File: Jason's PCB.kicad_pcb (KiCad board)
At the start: 2 copper layers, 9 parts, among them U1 Elite-C

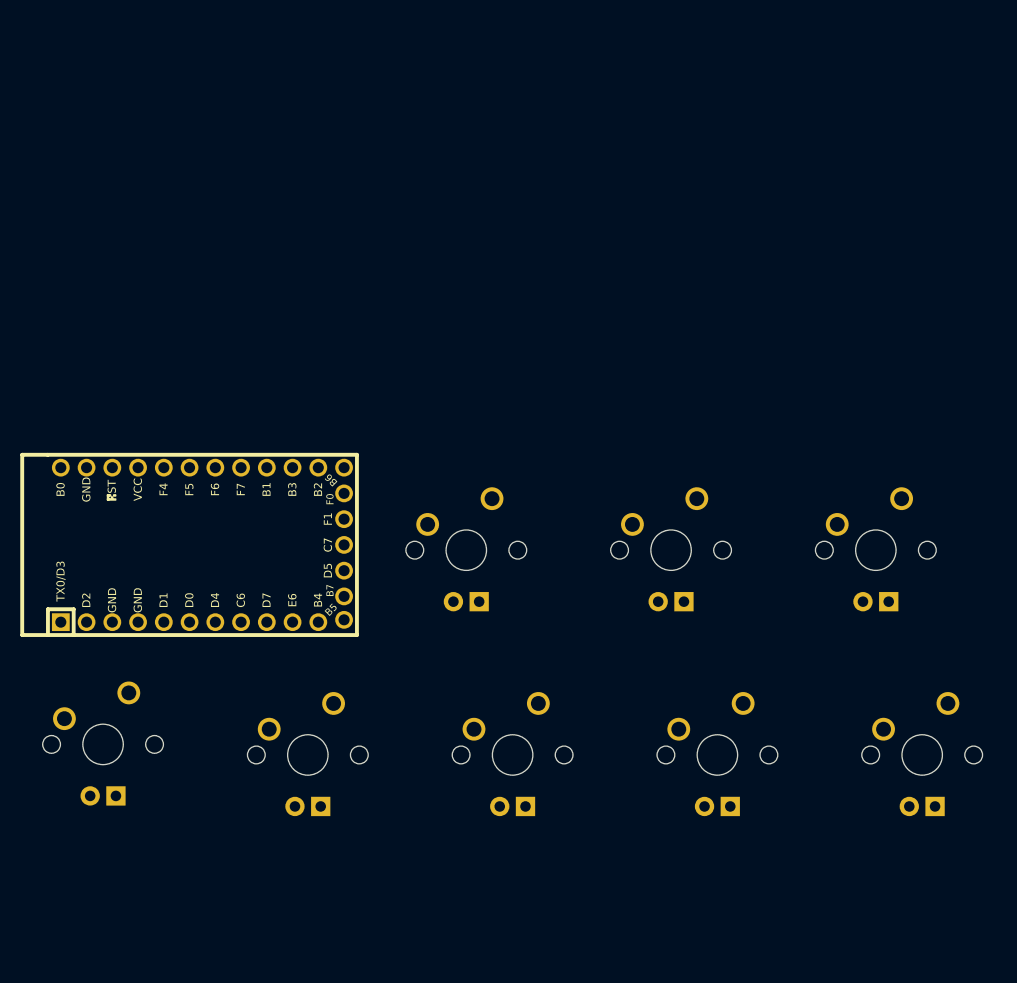
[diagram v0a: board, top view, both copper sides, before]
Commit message: Schematic/PCB General Shape
-Added 2 rotary encoder
-Simplified PCB. No need for diodes.
-Added outside edges of PCB
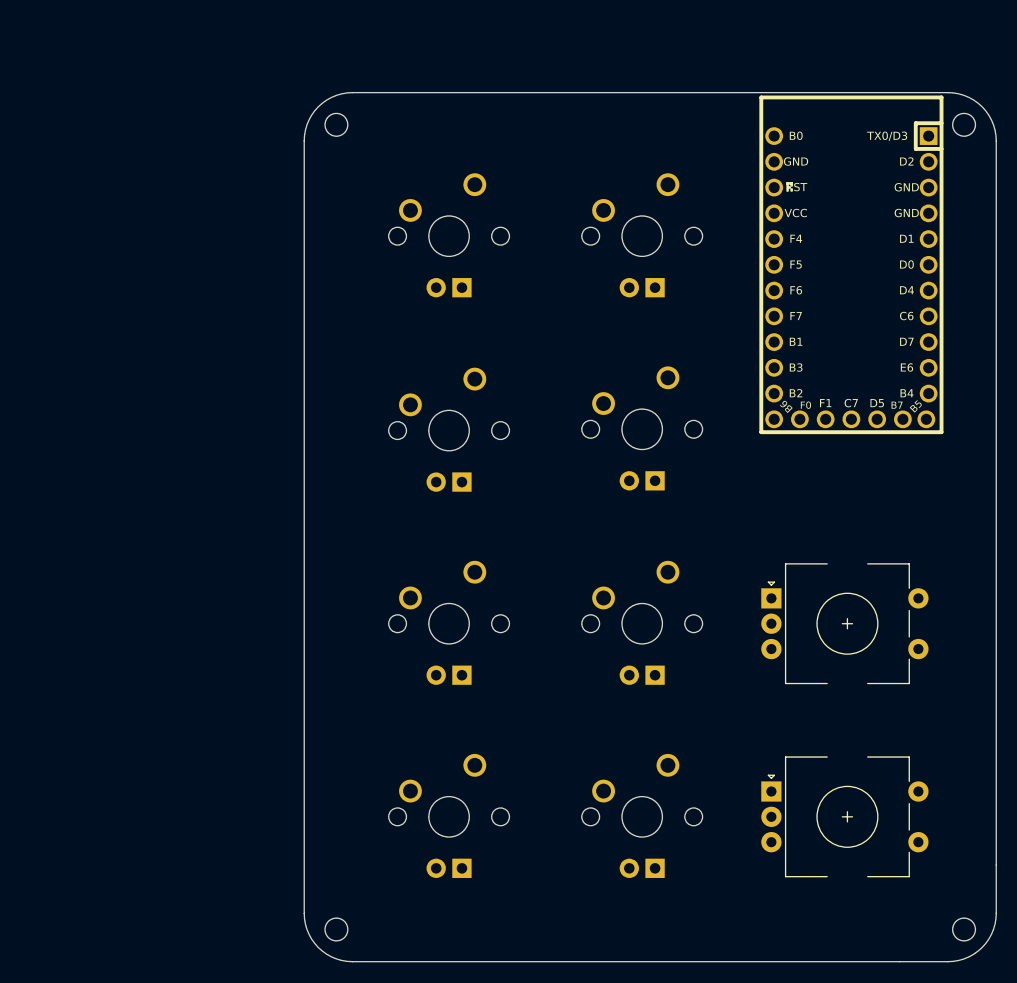
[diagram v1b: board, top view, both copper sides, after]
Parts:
- added SW_E1: Rotary_Encoder_Switch, Keebio-Parts:RotaryEncoder_EC11, F.Cu at (153.6, 73.0)
- added SW_E2: Rotary_Encoder_Switch, Keebio-Parts:RotaryEncoder_EC11, F.Cu at (153.6, 92.1)
- U1: moved to B.Cu
- moved U1 69.2 mm to (154.0, 38.9), turned to 270 degrees
- moved SW_A1 60.6 mm to (114.3, 34.8)
- moved SW_A2 35.5 mm to (133.3, 34.8)
- moved SW_B1 34.9 mm to (114.3, 54.0)
- moved SW_D2 28.3 mm to (133.3, 92.1)
- moved SW_D1 27.2 mm to (114.3, 92.1)
- moved SW_C2 24.2 mm to (133.3, 73.0)
- moved SW_C1 14.4 mm to (114.3, 73.0)
- moved SW_B2 12.3 mm to (133.3, 53.8)
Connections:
- SW_A2 pad 1: Net-(SW_A2-Pad1) -> SWA2
- U1 pad 11: Net-(U1-Pad11) -> Enc1A
- U1 pad 12: Net-(U1-Pad12) -> Enc1B
- U1 pad 13: Net-(U1-Pad13) -> Enc2B
- U1 pad 14: Net-(U1-Pad14) -> Enc2A
- U1 pad 15: Net-(U1-Pad15) -> SWD3
- U1 pad 16: Net-(U1-Pad16) -> SWD2
- U1 pad 17: SWD2 -> SWD1
- U1 pad 18: SWD1 -> SWC3
- U1 pad 7: SWB1 -> Net-(U1-Pad7)
- U1 pad 8: SWB2 -> SWB1
- U1 pad 9: Net-(U1-Pad9) -> SWB2
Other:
- board outline added: 68.3 x 85.7 mm

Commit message: Adjusted rotary encoder placements
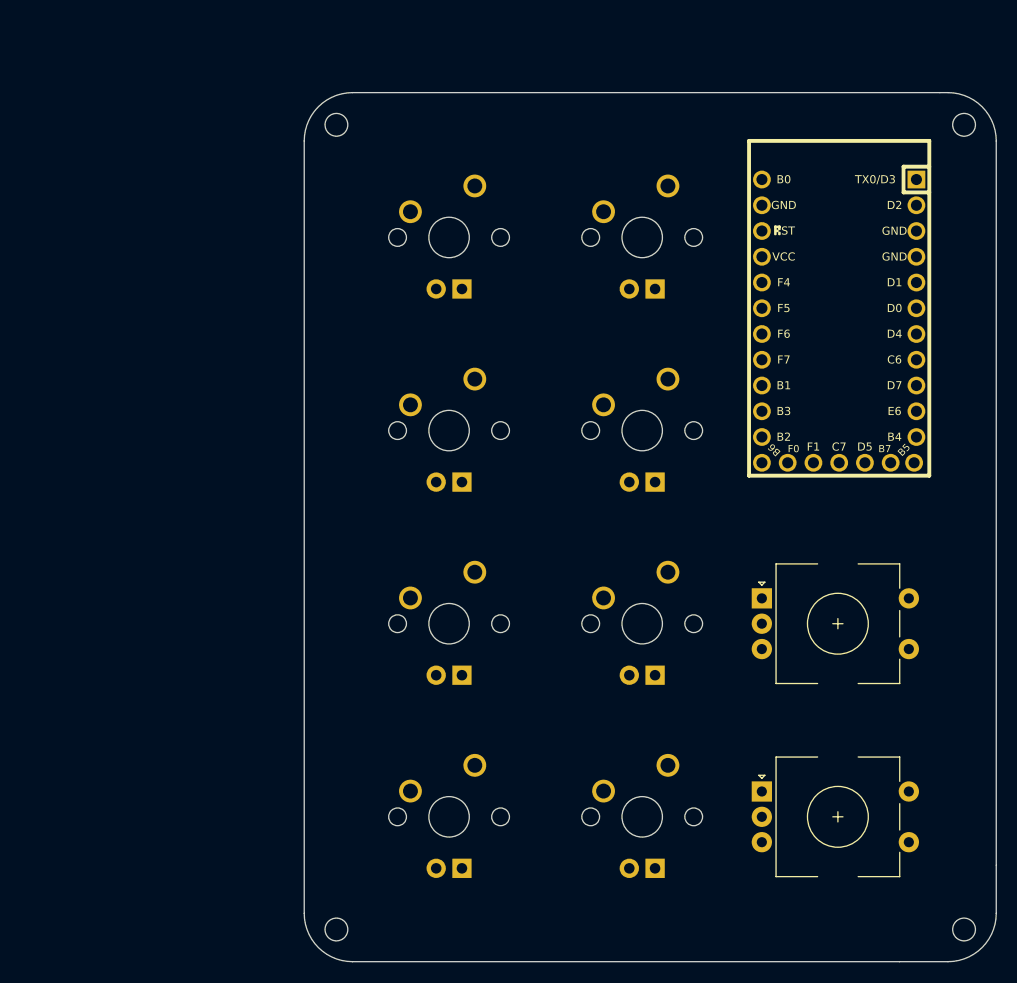
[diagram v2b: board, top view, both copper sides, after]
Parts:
- moved U1 4.45 mm to (152.8, 43.2)
- moved SW_E1 0.94 mm to (152.7, 73.0)
- moved SW_E2 0.94 mm to (152.7, 92.1)
- moved SW_B2 0.13 mm to (133.3, 54.0)
- moved SW_A1 0.13 mm to (114.3, 34.9)
- moved SW_A2 0.13 mm to (133.3, 34.9)

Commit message: Edge cut changes
- Consistent 4.76 mm bezel around switches
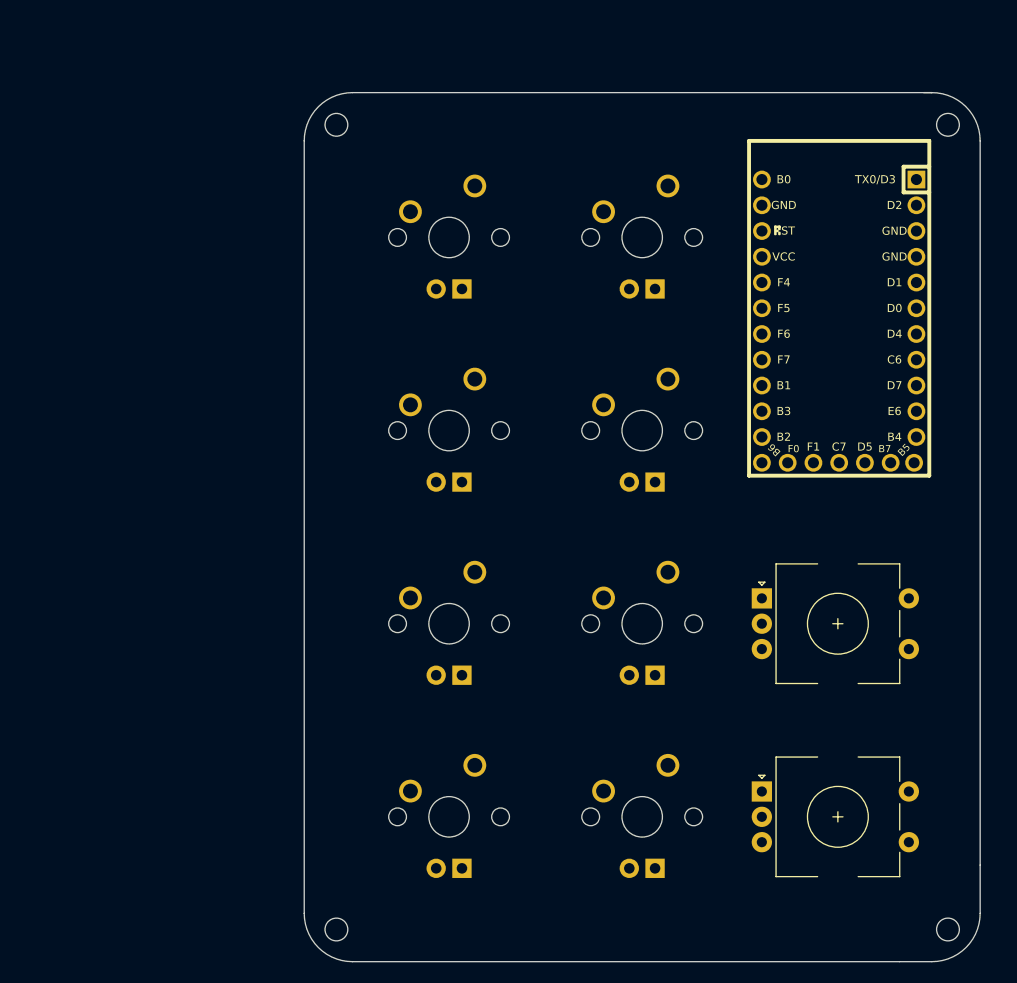
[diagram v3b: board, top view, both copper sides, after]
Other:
- board size 68.3 x 85.7 mm -> 66.7 x 85.7 mm

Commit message: Routing
-Changed nets in schematic to make routing easier
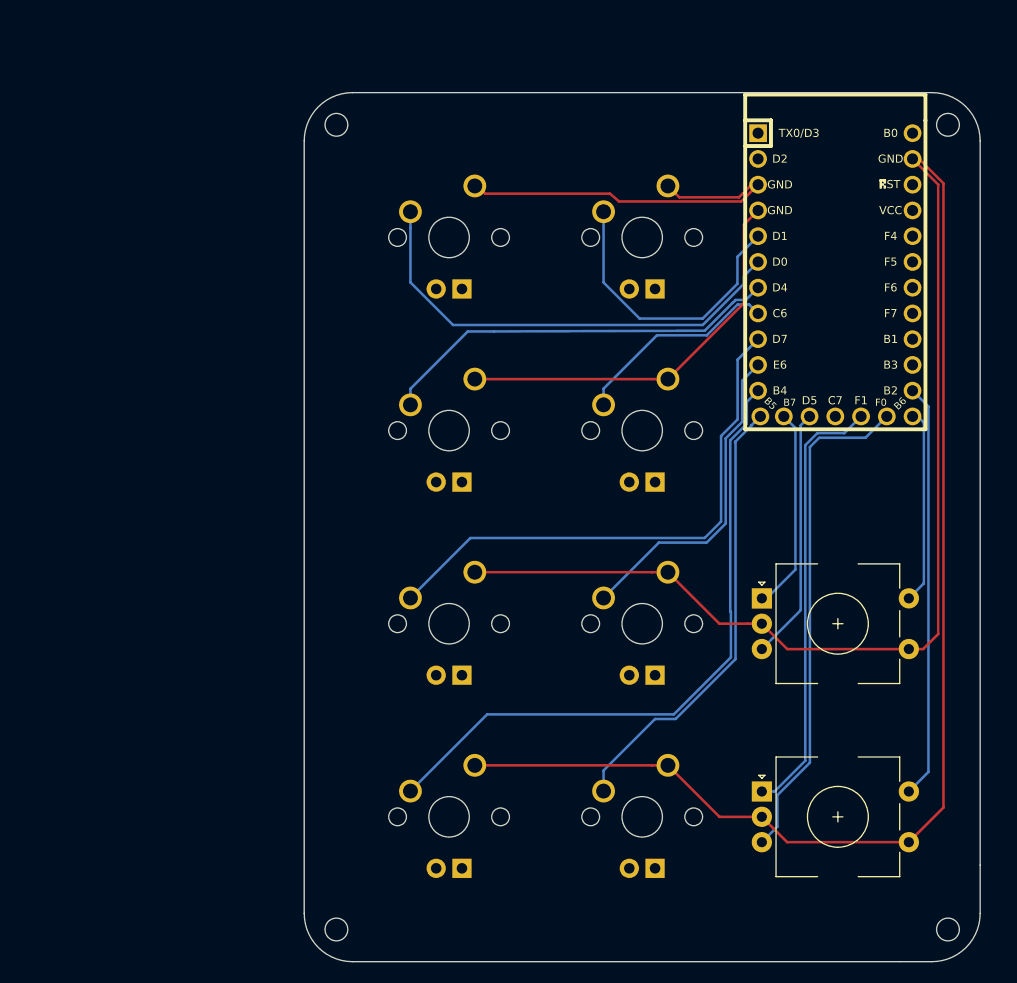
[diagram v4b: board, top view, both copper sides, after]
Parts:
- U1: moved to F.Cu
- moved U1 4.59 mm to (152.4, 38.6)
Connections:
- U1 pad 10: Net-(U1-Pad10) -> SWC2
- U1 pad 11: Enc1A -> SWD1
- U1 pad 12: Enc1B -> SWD2
- U1 pad 13: Enc2B -> SWC3
- U1 pad 14: Enc2A -> SWD3
- U1 pad 15: SWD3 -> Net-(U1-Pad15)
- U1 pad 16: SWD2 -> Net-(U1-Pad16)
- U1 pad 17: SWD1 -> Net-(U1-Pad17)
- U1 pad 18: SWC3 -> Net-(U1-Pad18)
- U1 pad 19: SWC2 -> Net-(U1-Pad19)
- U1 pad 20: SWC1 -> Net-(U1-Pad20)
- U1 pad 25: Net-(U1-Pad25) -> Enc1A
- U1 pad 26: Net-(U1-Pad26) -> Enc1B
- U1 pad 28: Net-(U1-Pad28) -> Enc2A
- U1 pad 29: Net-(U1-Pad29) -> Enc2B
- U1 pad 5: SWA1 -> SWA2
- U1 pad 6: SWA2 -> SWA1
- U1 pad 7: Net-(U1-Pad7) -> SWB1
- U1 pad 8: SWB1 -> SWB2
- U1 pad 9: SWB2 -> SWC1
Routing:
- net GND: track 0.00 -> 292.2 mm
- net SWD1: track 0.00 -> 64.5 mm
- net SWC1: track 0.00 -> 53.3 mm
- net Enc2B: track 0.00 -> 49.8 mm
- net SWA1: track 0.00 -> 46.0 mm
- net SWD2: track 0.00 -> 44.6 mm
- net Enc2A: track 0.00 -> 44.4 mm
- net SWD3: track 0.00 -> 41.0 mm
- net SWB1: track 0.00 -> 40.0 mm
- net SWC2: track 0.00 -> 32.1 mm
- net SWA2: track 0.00 -> 28.6 mm
- net Enc1B: track 0.00 -> 24.9 mm
- net Enc1A: track 0.00 -> 22.2 mm
- net SWB2: track 0.00 -> 20.6 mm
- net SWC3: track 0.00 -> 19.3 mm
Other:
- outline, holes or cut-outs redrawn
- net class Default: trace_width 0.25 -> 0.254
- net class Power added: clearance 0.2, trace_width 0.381, via_dia 0.8, via_drill 0.4

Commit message: More routing changes
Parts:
- moved U1 13.8 mm to (138.6, 38.7)
- moved SW_A1 13.8 mm to (100.5, 35.1)
- moved SW_B1 13.8 mm to (100.5, 54.1)
- moved SW_C1 13.8 mm to (100.5, 73.2)
- moved SW_D1 13.8 mm to (100.5, 92.2)
- moved SW_A2 13.8 mm to (119.5, 35.1)
- moved SW_B2 13.8 mm to (119.5, 54.1)
- moved SW_C2 13.8 mm to (119.5, 73.2)
- moved SW_D2 13.8 mm to (119.5, 92.2)
- moved SW_E1 13.8 mm to (138.8, 73.2)
- moved SW_E2 13.8 mm to (138.8, 92.2)

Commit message: gerber updates
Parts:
- moved SW_E1 12.4 mm to (128.8, 65.9)
- moved SW_E2 12.4 mm to (128.8, 85.0)
- moved SW_C2 12.4 mm to (109.5, 65.9)
- moved SW_D2 12.4 mm to (109.5, 85.0)
- moved SW_A2 12.4 mm to (109.5, 27.8)
- moved SW_B2 12.4 mm to (109.5, 46.9)
- moved SW_C1 12.4 mm to (90.4, 65.9)
- moved SW_D1 12.4 mm to (90.4, 85.0)
- moved SW_A1 12.4 mm to (90.4, 27.8)
- moved U1 12.4 mm to (128.5, 31.5)
- moved SW_B1 12.4 mm to (90.4, 46.9)
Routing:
- net (no net): vias 0 -> 4
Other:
- outline, holes or cut-outs redrawn
